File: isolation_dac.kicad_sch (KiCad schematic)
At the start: 12 parts, among them IC1 DAC63204RTERQ1, IC2 ISO7641FMDWR, T1 760390014, U3 TPS76333

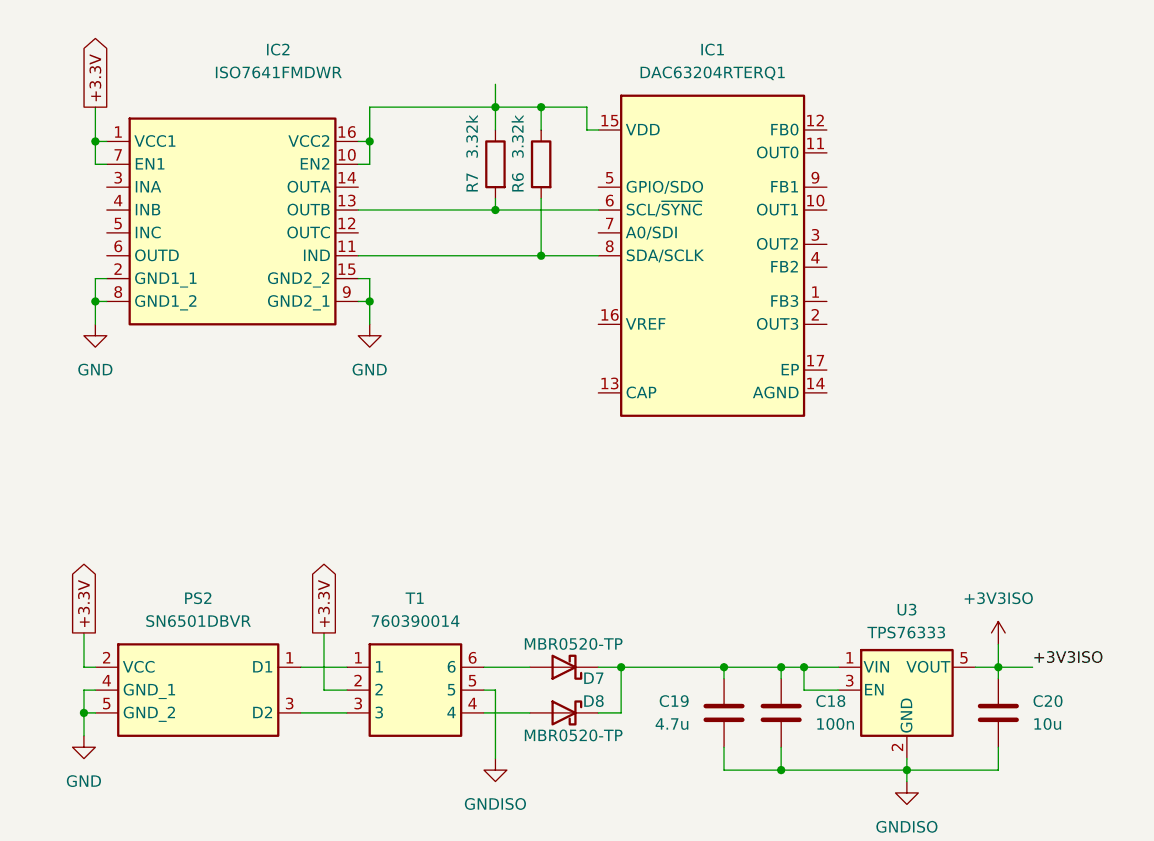
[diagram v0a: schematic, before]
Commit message: fix: adding isolation and HV pages
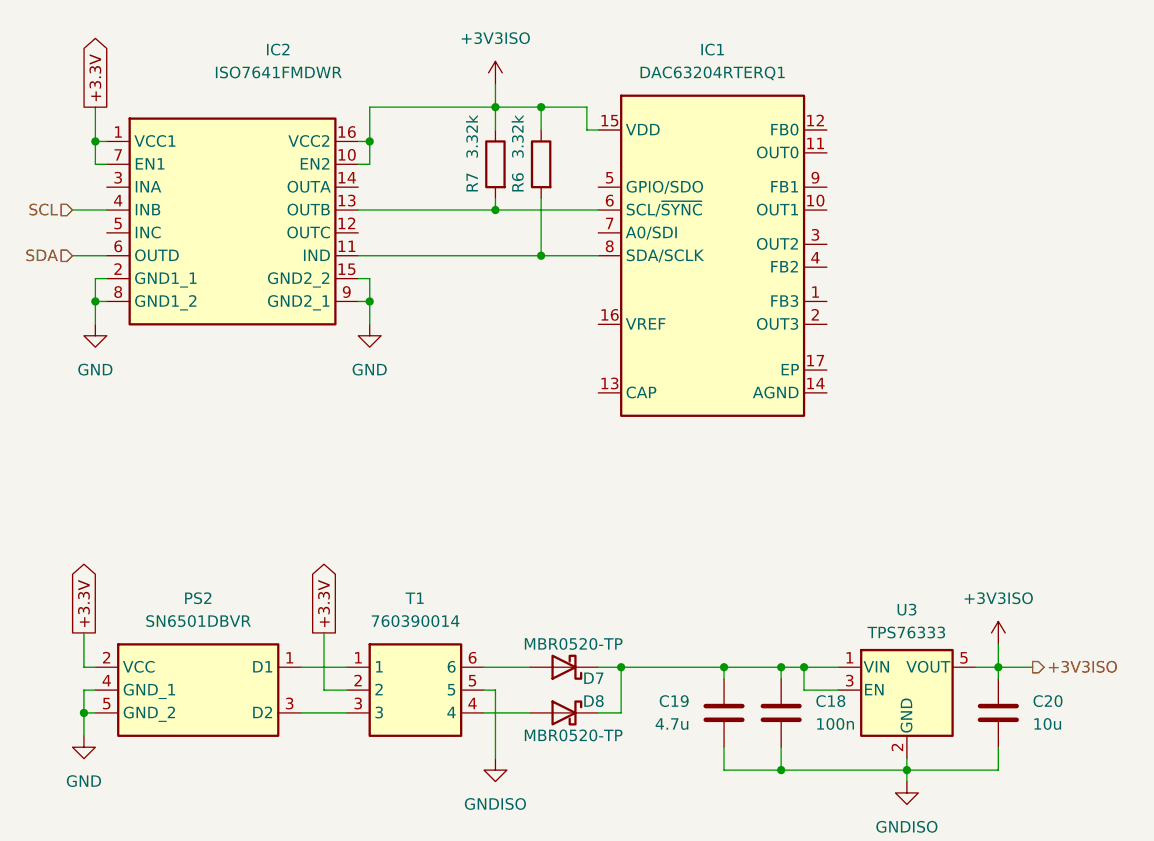
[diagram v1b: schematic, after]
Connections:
- net +3V3ISO: now also IC1.15 (VDD), IC2.10 (EN2), IC2.16 (VCC2), R6.1, R7.1
- net SCL: now reaches IC2.4 (INB)
- net SDA: now reaches IC2.6 (OUTD)
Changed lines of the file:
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@@
+	(wire
+		(pts
+			(xy 54.61 72.39) (xy 58.42 72.39)
+		)
+		(stroke
+			(width 0)
+			(type default)
+		)
+	)
 	(wire
 		(pts
@@
 	(wire
 		(pts
-			(xy 57.15 123.19) (xy 55.88 123.19)
+			(xy 54.61 77.47) (xy 58.42 77.47)
 		)
 		(stroke
@@
 	(wire
 		(pts
-			(xy 58.42 80.01) (xy 57.15 80.01)
+			(xy 57.15 123.19) (xy 55.88 123.19)
 		)
 		(stroke
@@
 	(wire
 		(pts
-			(xy 133.35 132.08) (xy 133.35 134.62)
+			(xy 58.42 80.01) (xy 57.15 80.01)
 		)
 		(stroke
@@
 	(wire
 		(pts
-			(xy 101.6 60.96) (xy 101.6 63.5)
+			(xy 133.35 132.08) (xy 133.35 134.62)
 		)
 		(stroke
@@
 	(wire
 		(pts
-			(xy 101.6 72.39) (xy 113.03 72.39)
+			(xy 101.6 60.96) (xy 101.6 63.5)
 		)
 		(stroke
@@
 	(wire
 		(pts
-			(xy 101.6 60.96) (xy 101.6 58.42)
+			(xy 101.6 72.39) (xy 113.03 72.39)
 		)
 		(stroke
@@
 	(wire
 		(pts
-			(xy 101.6 71.12) (xy 101.6 72.39)
+			(xy 101.6 60.96) (xy 101.6 58.42)
 		)
 		(stroke
@@
 	(wire
 		(pts
-			(xy 133.35 134.62) (xy 147.32 134.62)
+			(xy 101.6 71.12) (xy 101.6 72.39)
 		)
 		(stroke
@@
 	(wire
 		(pts
-			(xy 86.36 82.55) (xy 87.63 82.55)
+			(xy 133.35 134.62) (xy 147.32 134.62)
 		)
 		(stroke
@@
 	(wire
 		(pts
-			(xy 57.15 67.31) (xy 57.15 64.77)
+			(xy 86.36 82.55) (xy 87.63 82.55)
 		)
 		(stroke
@@
 	(wire
 		(pts
-			(xy 147.32 134.62) (xy 147.32 135.89)
+			(xy 57.15 67.31) (xy 57.15 64.77)
 		)
 		(stroke
@@
 	(wire
 		(pts
-			(xy 80.01 123.19) (xy 85.09 123.19)
+			(xy 147.32 134.62) (xy 147.32 135.89)
 		)
 		(stroke
@@
 	(wire
 		(pts
-			(xy 127 132.08) (xy 127 134.62)
+			(xy 80.01 123.19) (xy 85.09 123.19)
 		)
 		(stroke
@@
 	(wire
 		(pts
-			(xy 57.15 64.77) (xy 57.15 60.96)
+			(xy 127 132.08) (xy 127 134.62)
 		)
 		(stroke
@@
 	(wire
 		(pts
-			(xy 157.48 132.08) (xy 157.48 134.62)
+			(xy 57.15 64.77) (xy 57.15 60.96)
 		)
 		(stroke
@@
 	(wire
 		(pts
-			(xy 106.68 77.47) (xy 113.03 77.47)
+			(xy 157.48 132.08) (xy 157.48 134.62)
 		)
 		(stroke
@@
 	(wire
 		(pts
-			(xy 106.68 71.12) (xy 106.68 77.47)
+			(xy 106.68 77.47) (xy 113.03 77.47)
 		)
 		(stroke
@@
 		)
 	)
-	(label "+3V3ISO"
-		(at 161.29 123.19 0)
-		(fields_autoplaced yes)
-		(effects
-			(font
-				(size 1.27 1.27)
-			)
-			(justify left bottom)
+	(wire
+		(pts
+			(xy 106.68 71.12) (xy 106.68 77.47)
+		)
+		(stroke
+			(width 0)
+			(type default)
 		)
 	)
@@
 				(hide yes)
 			)
+		)
+	)
+	(hierarchical_label "SDA"
+		(shape input)
+		(at 54.61 77.47 180)
+		(fields_autoplaced yes)
+		(effects
+			(font
+				(size 1.27 1.27)
+			)
+			(justify right)
+		)
+	)
+	(hierarchical_label "+3V3ISO"
+		(shape output)
+		(at 161.29 123.19 0)
+		(fields_autoplaced yes)
+		(effects
+			(font
+				(size 1.27 1.27)
+			)
+			(justify left)
+		)
+	)
+	(hierarchical_label "SCL"
+		(shape input)
+		(at 54.61 72.39 180)
+		(fields_autoplaced yes)
+		(effects
+			(font
+				(size 1.27 1.27)
+			)
+			(justify right)
 		)
 	)
@@
 					(unit 1)
 				)
+			)
+		)
+	)
+	(symbol
+		(lib_id "power:+3V3")
+		(at 101.6 58.42 0)
+		(unit 1)
+		(exclude_from_sim no)
+		(in_bom yes)
+		(on_board yes)
+		(dnp no)
+		(fields_autoplaced yes)
+		(property "Reference" "#PWR038"
+			(at 101.6 62.23 0)
+			(effects
+				(font
+					(size 1.27 1.27)
+				)
+				(hide yes)
+			)
+		)
+		(property "Value" "+3V3ISO"
+			(at 101.6 53.34 0)
+			(effects
+				(font
+					(size 1.27 1.27)
+				)
+			)
+		)
+		(property "Footprint" ""
+			(at 101.6 58.42 0)
+			(effects
+				(font
+					(size 1.27 1.27)
+				)
+				(hide yes)
+			)
+		)
+		(property "Datasheet" ""
+			(at 101.6 58.42 0)
+			(effects
+				(font
+					(size 1.27 1.27)
+				)
+				(hide yes)
+			)
+		)
+		(property "Description" "Power symbol creates a global label with name \"+3V3\""
+			(at 101.6 58.42 0)
+			(effects
+				(font
+					(size 1.27 1.27)
+				)
+				(hide yes)
+			)
+		)
+		(pin "1"
+		)
+		(instances
+			(project "techstim-hardware"
+				(path "/1d5ae591-53a2-4652-87aa-0cddc0836341/6f1c9813-6d9b-43a0-a5d7-e66a0b6ca03e"
+					(reference "#PWR038")
+					(unit 1)
+				)

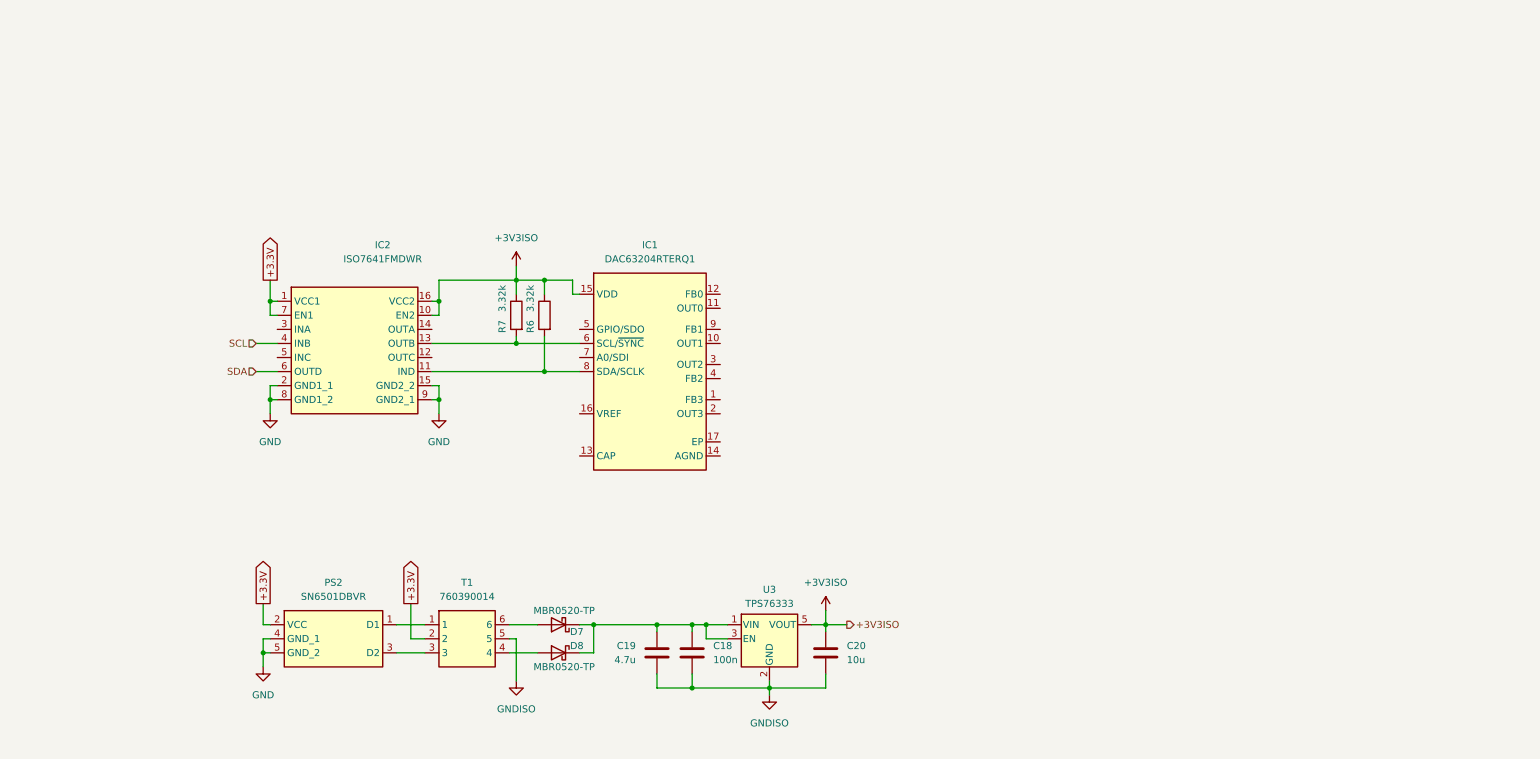
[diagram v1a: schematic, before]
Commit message: feat: adding isolation_dac sheet
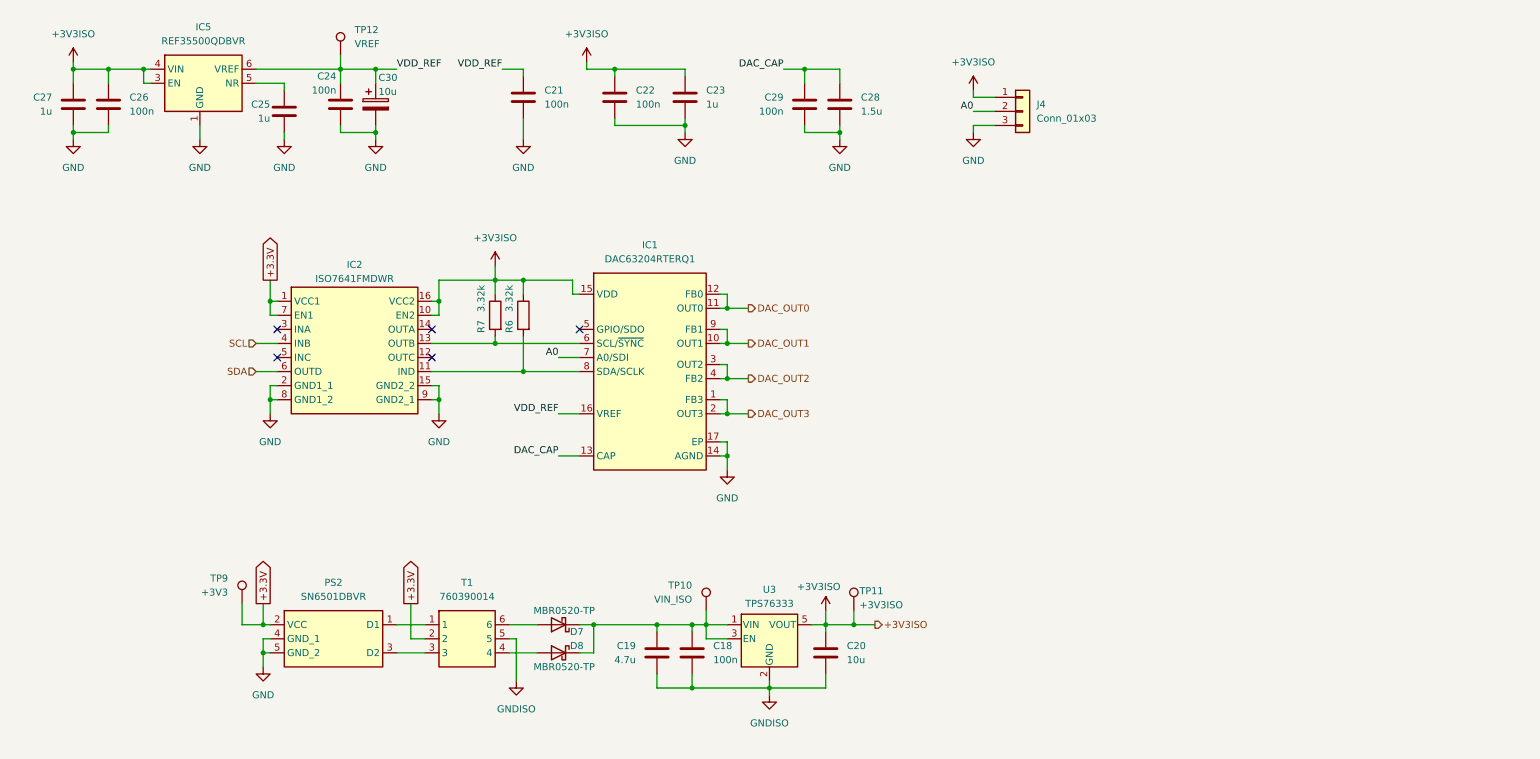
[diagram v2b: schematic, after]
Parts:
- added C21, C22, C24, C26, C29: 100n, Capacitor_SMD:C_0805_2012Metric_Pad1.18x1.45mm_HandSolder, symbol Device:C
- added C23, C25, C27: 1u, Capacitor_SMD:C_0805_2012Metric_Pad1.18x1.45mm_HandSolder, symbol Device:C
- added C28: 1.5u, Capacitor_SMD:C_0805_2012Metric_Pad1.18x1.45mm_HandSolder, symbol Device:C
- added C30: 10u, Capacitor_SMD:C_0805_2012Metric_Pad1.18x1.45mm_HandSolder, symbol Device:C_Polarized
- added IC5: REF35500QDBVR, Package_TO_SOT_SMD:SOT-23-6, symbol techstim:REF35500QDBVR
- added J4: Conn_01x03, Connector_PinHeader_2.54mm:PinHeader_1x03_P2.54mm_Vertical, symbol Connector_Generic:Conn_01x03
- added TP10: VIN_ISO, TestPoint:TestPoint_Pad_D1.0mm, symbol Connector:TestPoint
- added TP11: +3V3ISO, TestPoint:TestPoint_Pad_D1.0mm, symbol Connector:TestPoint
- added TP12: VREF, TestPoint:TestPoint_Pad_D1.0mm, symbol Connector:TestPoint
- added TP9: +3V3, TestPoint:TestPoint_Pad_D1.0mm, symbol Connector:TestPoint
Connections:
- net +3.3V: now also TP9.1
- net +3V3ISO: now also C22.2, C23.2, C26.2, C27.2, IC5.3 (EN), IC5.4 (VIN), J4.1 (Pin_1), TP11.1
- net GND: now also IC1.14 (AGND), IC1.17 (EP), C21.1, C22.1, C23.1, C24.1, C25.1, C26.1, C27.1, C28.1, C29.1, C30.2, IC5.1 (GND), IC5.2 (GND), J4.3 (Pin_3)
- net at C18.2, C19.1, D7.1 (K)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: now also TP10.1
- net DAC_OUT3: now reaches IC1.1 (FB3)
- net DAC_OUT3: now also IC1.2 (OUT3)
- net DAC_OUT1: now reaches IC1.10 (OUT1)
- net DAC_OUT1: now also IC1.9 (FB1)
- net DAC_OUT0: now reaches IC1.11 (OUT0)
- net DAC_OUT0: now also IC1.12 (FB0)
- net DAC_CAP: now reaches IC1.13 (CAP)
- net DAC_CAP: now also C28.2, C29.2
- net VDD_REF: now reaches IC1.16 (VREF)
- net VDD_REF: now also C21.2, C24.2, C30.1, IC5.6 (VREF), TP12.1
- net DAC_OUT2: now reaches IC1.3 (OUT2)
- net DAC_OUT2: now also IC1.4 (FB2)
- net A0: now reaches IC1.7 (A0/SDI)
- net A0: now also J4.2 (Pin_2)
- new net: C25.2, IC5.5 (NR)
- no-connect marks 0 -> 5
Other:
- moved on the sheet: R6, R7

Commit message: fix: using REF4096 for 12 bits
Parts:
- IC5: value REF35500QDBVR -> REF35409QDBVR; MFN (none) -> Texas Instruments; MFP (none) -> REF35500QDBVR; Manufacturer_Name Texas Instruments -> (none); Manufacturer_Part_Number REF35500QDBVR -> (none); S1PL (none) -> https://eu.mouser.com/ProductDetail/Texas-Instruments/REF35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; S1PN (none) -> Mouser
- T1: value 760390014 -> 760390015; MFN (none) -> Wurth Elektronik; MFP (none) -> 760390015; Manufacturer_Name Wurth Elektronik -> (none); Manufacturer_Part_Number 760390014 -> (none); Mouser Part Number 710-760390014 -> 710-760390050; S1PL (none) -> https://eu.mouser.com/ProductDetail/Wurth-Elektronik/760390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; S1PN (none) -> Mouser
- TP11: value +3V3ISO -> +5VISO
- U3: value TPS76333 -> TPS76350DBVRG4; MFN (none) -> Texas Instruments; MFP (none) -> TPS76350DBVRG4; S1PL (none) -> https://eu.mouser.com/ProductDetail/Texas-Instruments/TPS76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; S1PN (none) -> Mouser
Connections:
- net +3V3ISO renamed +5VISO
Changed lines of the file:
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@@
 		)
 	)
-	(hierarchical_label "+3V3ISO"
+	(hierarchical_label "+5VISO"
 		(shape output)
 		(at 166.37 123.19 0)
@@
 			)
 		)
-		(property "Value" "REF35500QDBVR"
+		(property "Value" "REF35409QDBVR"
 			(at 45.085 17.78 0)
 			(effects
@@
 			)
 		)
-		(property "Manufacturer_Name" "Texas Instruments"
-			(at 64.77 715.24 0)
+		(property "MFN" "Texas Instruments"
+			(at 38.1 20.32 0)
 			(effects
 				(font
 					(size 1.27 1.27)
 				)
-				(justify left top)
 				(hide yes)
 			)
 		)
-		(property "Manufacturer_Part_Number" "REF35500QDBVR"
-			(at 64.77 815.24 0)
+		(property "MFP" "REF35500QDBVR"
+			(at 38.1 20.32 0)
+			(effects
+				(font
+					(size 1.27 1.27)
+				)
+				(hide yes)
+			)
+		)
+		(property "S1PN" "Mouser"
+			(at 38.1 20.32 0)
+			(effects
+				(font
+					(size 1.27 1.27)
+				)
+				(hide yes)
+			)
+		)
+		(property "S1PL" "https://eu.mouser.com/ProductDetail/Texas-Instruments/REF35409QDBVR?qs=Jm2GQyTW%2FbgBTryVLY6N3g%3D%3D"
+			(at 38.1 20.32 0)
 			(effects
 				(font
 					(size 1.27 1.27)
 				)
-				(justify left top)
 				(hide yes)
 			)
@@
 			)
 		)
-		(property "Value" "+3V3ISO"
+		(property "Value" "+5VISO"
 			(at 163.576 119.634 0)
 			(effects
@@
 			)
 		)
-		(property "Value" "+3V3ISO"
+		(property "Value" "+5VISO"
 			(at 184.15 21.59 0)
 			(effects
@@
 			)
 		)
-		(property "Value" "TPS76333"
+		(property "Value" "TPS76350DBVRG4"
 			(at 147.32 119.38 0)
 			(effects
@@
 			)
 		)
-		(property "Datasheet" "http://www.ti.com/lit/ds/symlink/tps763.pdf"
+		(property "Datasheet" "https://www.ti.com/lit/gpn/tps763"
+			(at 147.32 125.73 0)
+			(effects
+				(font
+					(size 1.27 1.27)
+				)
+				(hide yes)
+			)
+		)
+		(property "Description" "Low power 150mA LDO 5V fixed output voltage, SOT-23-5"
+			(at 147.32 125.73 0)
+			(effects
+				(font
+					(size 1.27 1.27)
+				)
+				(hide yes)
+			)
+		)
+		(property "MFN" "Texas Instruments"
 			(at 147.32 125.73 0)
 			(effects
@@
 			)
 		)
-		(property "Description" "Low power 150mA LDO 3.3V fixed output voltage, SOT-23-5"
+		(property "MFP" "TPS76350DBVRG4"
+			(at 147.32 125.73 0)
+			(effects
+				(font
+					(size 1.27 1.27)
+				)
+				(hide yes)
+			)
+		)
+		(property "S1PN" "Mouser"
+			(at 147.32 125.73 0)
+			(effects
+				(font
+					(size 1.27 1.27)
+				)
+				(hide yes)
+			)
+		)
+		(property "S1PL" "https://eu.mouser.com/ProductDetail/Texas-Instruments/TPS76350DBVRG4?qs=6zVL%252ByCp0mrPdp%252BxKum%252BJw%3D%3D"
 			(at 147.32 125.73 0)
 			(effects
@@
 			)
 		)
-		(property "Value" "760390014"
+		(property "Value" "760390015"
 			(at 92.71 118.11 0)
 			(effects
@@
 			)
 		)
-		(property "Mouser Part Number" "710-760390014"
+		(property "Mouser Part Number" "710-760390050"
 			(at 104.14 615.57 0)
 			(effects
@@
 			)
 		)
-		(property "Manufacturer_Name" "Wurth Elektronik"
-			(at 104.14 815.57 0)
-			(effects
-				(font
-					(size 1.27 1.27)
-				)
-				(justify left top)
-				(hide yes)
-			)
-		)
-		(property "Manufacturer_Part_Number" "760390014"
-			(at 104.14 915.57 0)
-			(effects
-				(font
-					(size 1.27 1.27)
-				)
-				(justify left top)
-				(hide yes)
-			)
-		)
-		(property "MFN" ""
+		(property "MFN" "Wurth Elektronik"
 			(at 87.63 120.65 0)
 			(effects
@@
 			)
 		)
-		(property "MFP" ""
+		(property "MFP" "760390015"
 			(at 87.63 120.65 0)
 			(effects
@@
 			)
 		)
-		(property "S1PN" ""
+		(property "S1PN" "Mouser"
 			(at 87.63 120.65 0)
 			(effects
@@
 			)
 		)
-		(property "S1PL" ""
+		(property "S1PL" "https://eu.mouser.com/ProductDetail/Wurth-Elektronik/760390015?qs=wElim4iM2pjOQCmk%252B8YbFA%3D%3D"
 			(at 87.63 120.65 0)
 			(effects
@@
 			)
 		)
-		(property "Value" "+3V3ISO"
+		(property "Value" "+5VISO"
 			(at 156.21 116.332 0)
 			(effects
@@
 			)
 		)
-		(property "Value" "+3V3ISO"
+		(property "Value" "+5VISO"
 			(at 21.59 16.51 0)
 			(effects
@@
 			)
 		)
-		(property "Value" "+3V3ISO"
+		(property "Value" "+5VISO"
 			(at 114.3 16.51 0)
 			(effects
@@
 			)
 		)
-		(property "Value" "+3V3ISO"
+		(property "Value" "+5VISO"
 			(at 97.79 53.34 0)
 			(effects
